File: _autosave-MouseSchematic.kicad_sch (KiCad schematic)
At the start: 67 parts, among them IC1 AZ1117IH-3.3TRG1, J1 Right Header, J2 Left Header, J4 JST1, J5 JST2, J6 Programming Header, Q1 IR Receiver, Q2 IR Receiver, Q3 IR Receiver, Q4 IR Receiver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

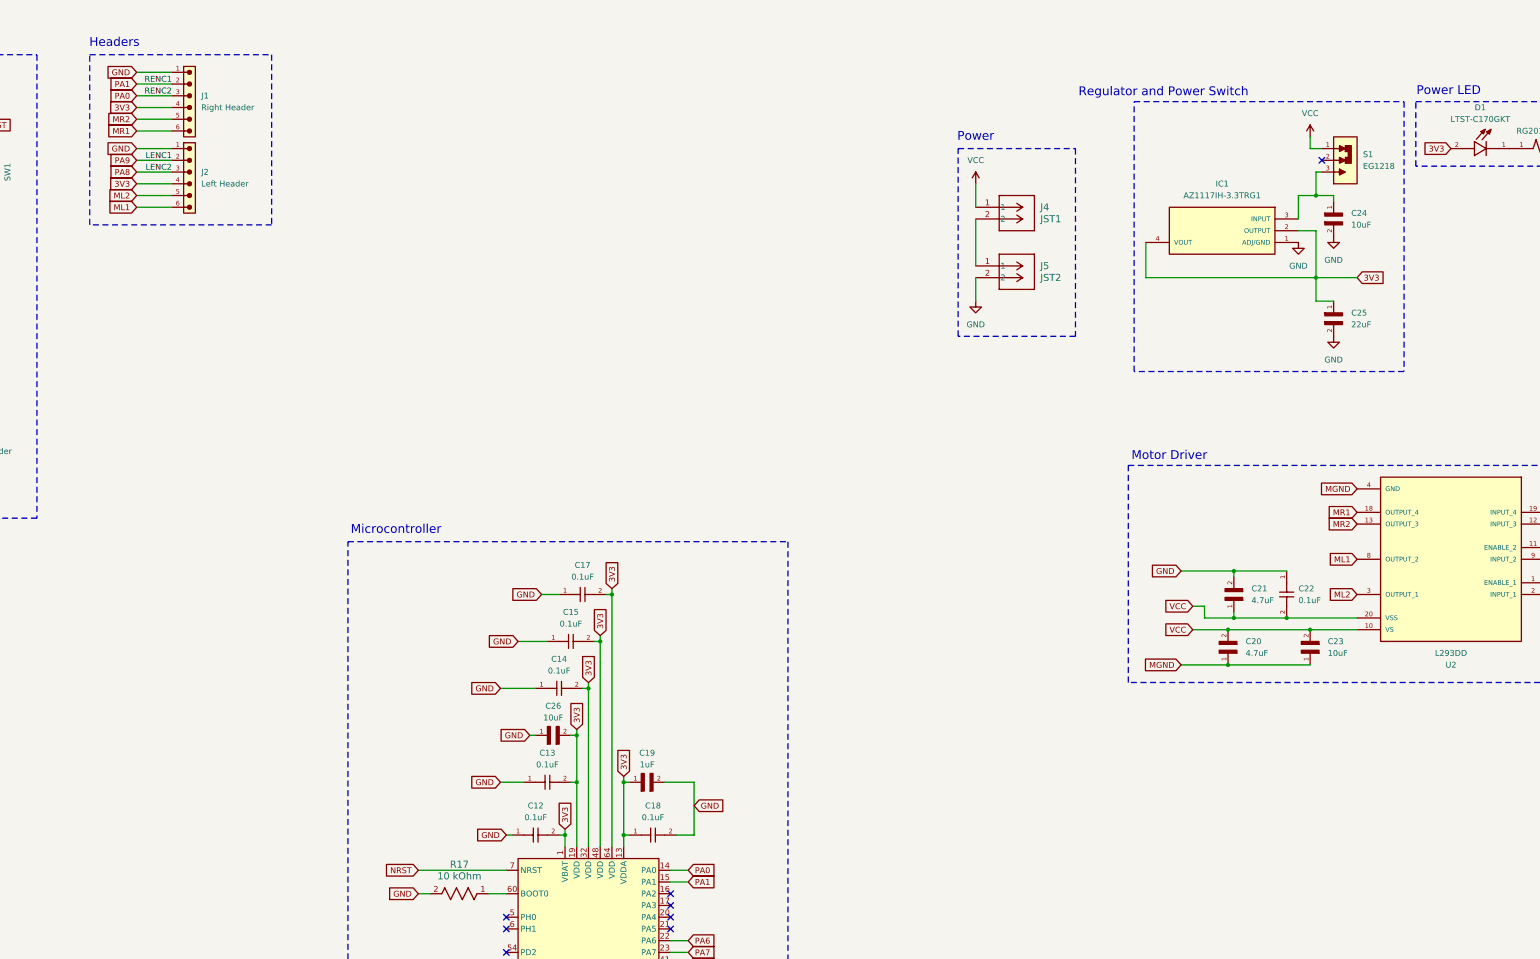
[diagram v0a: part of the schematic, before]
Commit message: Started layout (laid out 1 IR sensor/emitter pair, motor driver, and put components in general location)
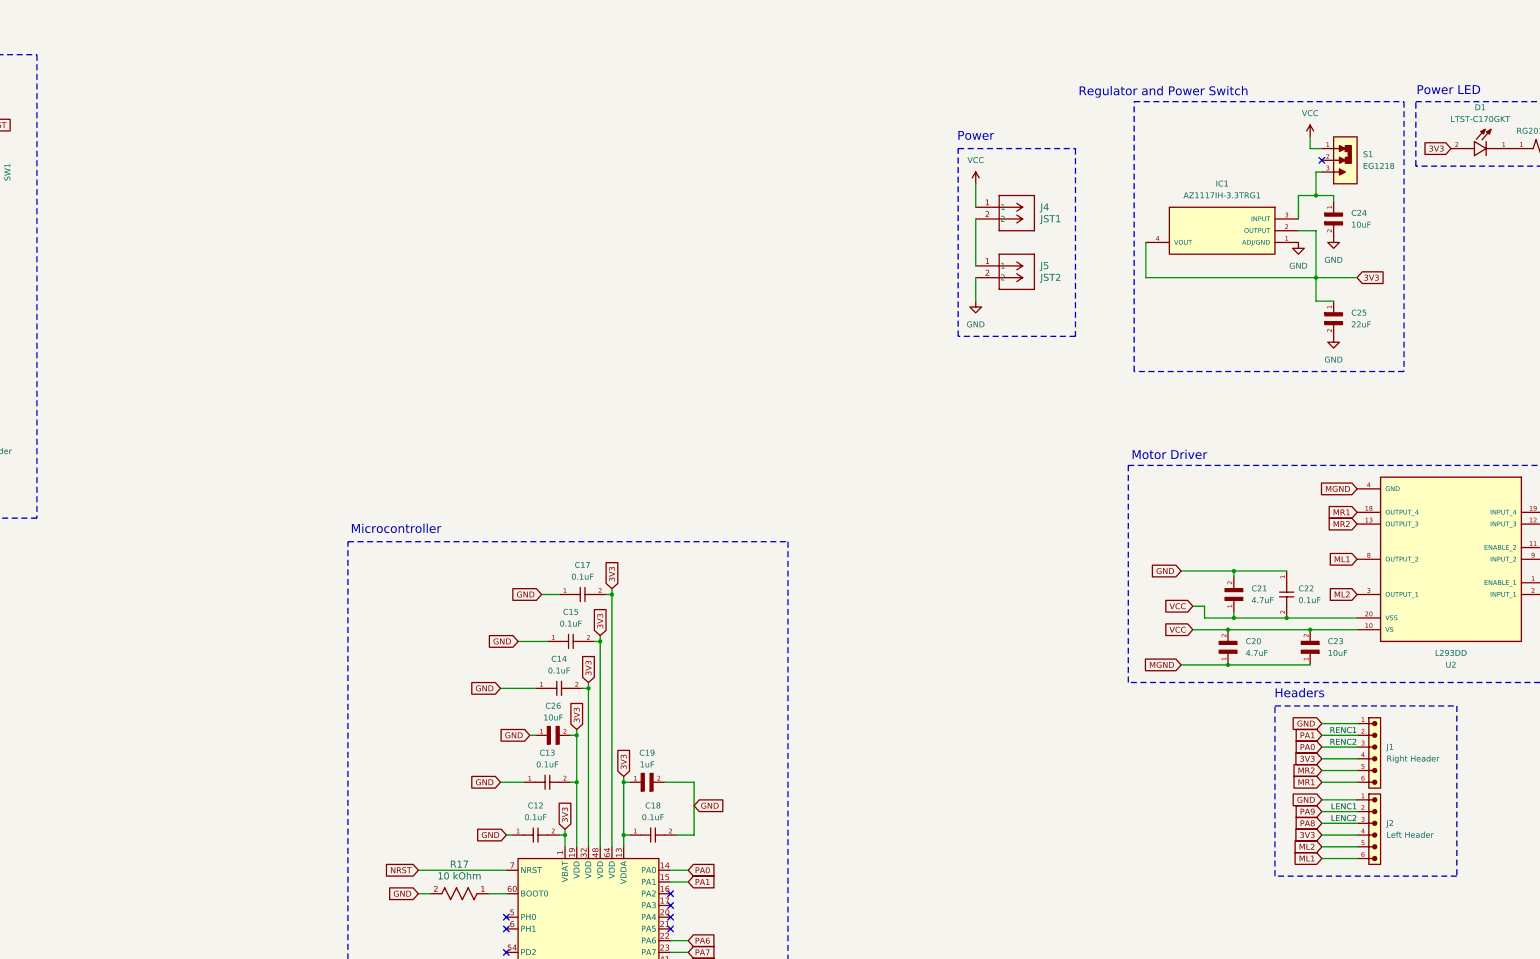
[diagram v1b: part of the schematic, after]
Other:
- moved on the sheet: J1, J2
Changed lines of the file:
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@@
 	)
 	(rectangle
-		(start 191.77 29.21)
-		(end 231.14 66.04)
+		(start 448.31 170.18)
+		(end 487.68 207.01)
 		(stroke
 			(width 0)
@@
 	(text "Headers"
 		(exclude_from_sim no)
-		(at 197.104 26.67 0)
+		(at 453.644 167.64 0)
 		(effects
 			(font
@@
 	(wire
 		(pts
-			(xy 201.93 43.18) (xy 209.55 43.18)
+			(xy 458.47 184.15) (xy 466.09 184.15)
 		)
 		(stroke
@@
 	(wire
 		(pts
-			(xy 201.93 62.23) (xy 209.55 62.23)
+			(xy 458.47 203.2) (xy 466.09 203.2)
 		)
 		(stroke
@@
 	(wire
 		(pts
-			(xy 201.93 35.56) (xy 209.55 35.56)
+			(xy 458.47 176.53) (xy 466.09 176.53)
 		)
 		(stroke
@@
 	(wire
 		(pts
-			(xy 201.93 57.15) (xy 209.55 57.15)
+			(xy 458.47 198.12) (xy 466.09 198.12)
 		)
 		(stroke
@@
 	(wire
 		(pts
-			(xy 201.93 38.1) (xy 209.55 38.1)
+			(xy 458.47 179.07) (xy 466.09 179.07)
 		)
 		(stroke
@@
 	(wire
 		(pts
-			(xy 201.93 40.64) (xy 209.55 40.64)
+			(xy 458.47 181.61) (xy 466.09 181.61)
 		)
 		(stroke
@@
 	(wire
 		(pts
-			(xy 201.93 59.69) (xy 209.55 59.69)
+			(xy 458.47 200.66) (xy 466.09 200.66)
 		)
 		(stroke
@@
 	(wire
 		(pts
-			(xy 201.93 45.72) (xy 209.55 45.72)
+			(xy 458.47 186.69) (xy 466.09 186.69)
 		)
 		(stroke
@@
 	(wire
 		(pts
-			(xy 201.93 54.61) (xy 209.55 54.61)
+			(xy 458.47 195.58) (xy 466.09 195.58)
 		)
 		(stroke
@@
 	(wire
 		(pts
-			(xy 201.93 33.02) (xy 209.55 33.02)
+			(xy 458.47 173.99) (xy 466.09 173.99)
 		)
 		(stroke
@@
 	(wire
 		(pts
-			(xy 201.93 52.07) (xy 209.55 52.07)
+			(xy 458.47 193.04) (xy 466.09 193.04)
 		)
 		(stroke
@@
 	(wire
 		(pts
-			(xy 201.93 49.53) (xy 209.55 49.53)
+			(xy 458.47 190.5) (xy 466.09 190.5)
 		)
 		(stroke
@@
 	)
 	(label "LENC1"
-		(at 209.55 52.07 180)
+		(at 466.09 193.04 180)
 		(effects
 			(font
@@
 	)
 	(label "LENC2"
-		(at 209.55 54.61 180)
+		(at 466.09 195.58 180)
 		(effects
 			(font
@@
 	)
 	(label "RENC1"
-		(at 209.55 35.56 180)
+		(at 466.09 176.53 180)
 		(effects
 			(font
@@
 	)
 	(label "RENC2"
-		(at 209.55 38.1 180)
+		(at 466.09 179.07 180)
 		(effects
 			(font
@@
 	(global_label "MR2"
 		(shape input)
-		(at 201.93 43.18 180)
+		(at 458.47 184.15 180)
 		(fields_autoplaced yes)
 		(effects
@@
 		)
 		(property "Intersheetrefs" "${INTERSHEET_REFS}"
-			(at 195.0139 43.18 0)
+			(at 451.5539 184.15 0)
 			(effects
 				(font
@@
 	(global_label "GND"
 		(shape input)
-		(at 201.93 33.02 180)
+		(at 458.47 173.99 180)
 		(fields_autoplaced yes)
 		(effects
@@
 		)
 		(property "Intersheetrefs" "${INTERSHEET_REFS}"
-			(at 195.0743 33.02 0)
+			(at 451.6143 173.99 0)
 			(effects
 				(font
@@
 	(global_label "3V3"
 		(shape input)
-		(at 201.93 40.64 180)
+		(at 458.47 181.61 180)
 		(fields_autoplaced yes)
 		(effects
@@
 		)
 		(property "Intersheetrefs" "${INTERSHEET_REFS}"
-			(at 195.4372 40.64 0)
+			(at 451.9772 181.61 0)
 			(effects
 				(font
@@
 	(global_label "MR1"
 		(shape input)
-		(at 201.93 45.72 180)
+		(at 458.47 186.69 180)
 		(fields_autoplaced yes)
 		(effects
@@
 		)
 		(property "Intersheetrefs" "${INTERSHEET_REFS}"
-			(at 195.0139 45.72 0)
+			(at 451.5539 186.69 0)
 			(effects
 				(font
@@
 	(global_label "GND"
 		(shape input)
-		(at 201.93 49.53 180)
+		(at 458.47 190.5 180)
 		(fields_autoplaced yes)
 		(effects
@@
 		)
 		(property "Intersheetrefs" "${INTERSHEET_REFS}"
-			(at 195.0743 49.53 0)
+			(at 451.6143 190.5 0)
 			(effects
 				(font
@@
 	(global_label "PA0"
 		(shape input)
-		(at 201.93 38.1 180)
+		(at 458.47 179.07 180)
 		(fields_autoplaced yes)
 		(effects
@@
 		)
 		(property "Intersheetrefs" "${INTERSHEET_REFS}"
-			(at 195.3767 38.1 0)
+			(at 451.9167 179.07 0)
 			(effects
 				(font
@@
 	(global_label "ML1"
 		(shape input)
-		(at 201.93 62.23 180)
+		(at 458.47 203.2 180)
 		(fields_autoplaced yes)
 		(effects
@@
 		)
 		(property "Intersheetrefs" "${INTERSHEET_REFS}"
-			(at 195.2558 62.23 0)
+			(at 451.7958 203.2 0)
 			(effects
 				(font
@@
 	(global_label "PA9"
 		(shape input)
-		(at 201.93 52.07 180)
+		(at 458.47 193.04 180)
 		(fields_autoplaced yes)
 		(effects
@@
 		)
 		(property "Intersheetrefs" "${INTERSHEET_REFS}"
-			(at 195.3767 52.07 0)
+			(at 451.9167 193.04 0)
 			(effects
 				(font
@@
 	(global_label "3V3"
 		(shape input)
-		(at 201.93 57.15 180)
+		(at 458.47 198.12 180)
 		(fields_autoplaced yes)
 		(effects
@@
 		)
 		(property "Intersheetrefs" "${INTERSHEET_REFS}"
-			(at 195.4372 57.15 0)
+			(at 451.9772 198.12 0)
 			(effects
 				(font
@@
 	(global_label "PA8"
 		(shape input)
-		(at 201.93 54.61 180)
+		(at 458.47 195.58 180)
 		(fields_autoplaced yes)
 		(effects
@@
 		)
 		(property "Intersheetrefs" "${INTERSHEET_REFS}"
-			(at 195.3767 54.61 0)
+			(at 451.9167 195.58 0)
 			(effects
 				(font
@@
 	(global_label "PA1"
 		(shape input)
-		(at 201.93 35.56 180)
+		(at 458.47 176.53 180)
 		(fields_autoplaced yes)
 		(effects
@@
 		)
 		(property "Intersheetrefs" "${INTERSHEET_REFS}"
-			(at 195.3767 35.56 0)
+			(at 451.9167 176.53 0)
 			(effects
 				(font
@@
 	(global_label "ML2"
 		(shape input)
-		(at 201.93 59.69 180)
+		(at 458.47 200.66 180)
 		(fields_autoplaced yes)
 		(effects
@@
 		)
 		(property "Intersheetrefs" "${INTERSHEET_REFS}"
-			(at 195.2558 59.69 0)
+			(at 451.7958 200.66 0)
 			(effects
 				(font
@@
 	(symbol
 		(lib_id "Connector01x06_6130XX11121_61300611121:6130XX11121_61300611121")
-		(at 214.63 38.1 270)
+		(at 471.17 179.07 270)
 		(unit 1)
 		(exclude_from_sim no)
@@
 		(fields_autoplaced yes)
 		(property "Reference" "J1"
-			(at 215.9 38.0999 90)
+			(at 472.44 179.0699 90)
 			(effects
 				(font
@@
 		)
 		(property "Value" "Right Header"
-			(at 215.9 40.6399 90)
+			(at 472.44 181.6099 90)
 			(effects
 				(font
@@
 		)
 		(property "Footprint" "6130XX11121_61300611121:61300611121"
-			(at 214.63 38.1 0)
+			(at 471.17 179.07 0)
 			(effects
 				(font
@@
 		)
 		(property "Datasheet" ""
-			(at 214.63 38.1 0)
+			(at 471.17 179.07 0)
 			(effects
 				(font
@@
 		)
 		(property "Description" ""
-			(at 214.63 38.1 0)
+			(at 471.17 179.07 0)
 			(effects
 				(font
@@
 		)
 		(property "DigiKey_Part_Number" "732-5319-ND"
-			(at 214.63 38.1 0)
+			(at 471.17 179.07 0)
 			(effects
 				(font
@@
 		)
 		(property "SnapEDA_Link" "https://www.snapeda.com/parts/61300611121/Wurth+Electronics/view-part/?ref=snap"
-			(at 214.63 38.1 0)
+			(at 471.17 179.07 0)
 			(effects
 				(font
@@
 		)
 		(property "Description_1" "6 pins, 1 row, straight, gold plating"
-			(at 214.63 38.1 0)
+			(at 471.17 179.07 0)
 			(effects
 				(font
@@
 		)
 		(property "MF" "Wurth Electronics"
-			(at 214.63 38.1 0)
+			(at 471.17 179.07 0)
 			(effects
 				(font
@@
 		)
 		(property "Package" "None"
-			(at 214.63 38.1 0)
+			(at 471.17 179.07 0)
 			(effects
 				(font
@@
 		)
 		(property "Check_prices" "https://www.snapeda.com/parts/61300611121/Wurth+Electronics/view-part/?ref=eda"
-			(at 214.63 38.1 0)
+			(at 471.17 179.07 0)
 			(effects
 				(font
@@
 		)
 		(property "MP" "61300611121"
-			(at 214.63 38.1 0)
+			(at 471.17 179.07 0)
 			(effects
 				(font
@@
 	(symbol
 		(lib_id "Connector01x06_6130XX11121_61300611121:6130XX11121_61300611121")
-		(at 214.63 54.61 270)
+		(at 471.17 195.58 270)
 		(unit 1)
 		(exclude_from_sim no)
@@
 		(fields_autoplaced yes)
 		(property "Reference" "J2"
-			(at 215.9 54.6099 90)
+			(at 472.44 195.5799 90)
 			(effects
 				(font
@@
 		)
 		(property "Value" "Left Header"
-			(at 215.9 57.1499 90)
+			(at 472.44 198.1199 90)
 			(effects
 				(font
@@
 		)
 		(property "Footprint" "6130XX11121_61300611121:61300611121"
-			(at 214.63 54.61 0)
+			(at 471.17 195.58 0)
 			(effects
 				(font
@@
 		)
 		(property "Datasheet" ""
-			(at 214.63 54.61 0)
+			(at 471.17 195.58 0)
 			(effects
 				(font
@@
 		)
 		(property "Description" ""
-			(at 214.63 54.61 0)
+			(at 471.17 195.58 0)
 			(effects
 				(font
@@
 		)
 		(property "DigiKey_Part_Number" "732-5319-ND"
-			(at 214.63 54.61 0)
+			(at 471.17 195.58 0)
 			(effects
 				(font
@@
 		)
 		(property "SnapEDA_Link" "https://www.snapeda.com/parts/61300611121/Wurth+Electronics/view-part/?ref=snap"
-			(at 214.63 54.61 0)
+			(at 471.17 195.58 0)
 			(effects
 				(font
@@
 		)
 		(property "Description_1" "6 pins, 1 row, straight, gold plating"
-			(at 214.63 54.61 0)
+			(at 471.17 195.58 0)
 			(effects
 				(font
@@
 		)
 		(property "MF" "Wurth Electronics"
-			(at 214.63 54.61 0)
+			(at 471.17 195.58 0)
 			(effects
 				(font
@@
 		)
 		(property "Package" "None"
-			(at 214.63 54.61 0)
+			(at 471.17 195.58 0)
 			(effects
 				(font
@@
 		)
 		(property "Check_prices" "https://www.snapeda.com/parts/61300611121/Wurth+Electronics/view-part/?ref=eda"
-			(at 214.63 54.61 0)
+			(at 471.17 195.58 0)
 			(effects
 				(font
@@
 		)
 		(property "MP" "61300611121"
-			(at 214.63 54.61 0)
+			(at 471.17 195.58 0)
 			(effects
 				(font

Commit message: Added traces but now gotta move components a little further apart from each other to make room for fill zones
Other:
- moved on the sheet: J1, J2, R16, R3, R5, R7
